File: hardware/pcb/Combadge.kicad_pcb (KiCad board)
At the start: 2 copper layers, 33.7 x 31 mm, 38 parts, among them J1 UART, J2 GND, J3 TOUCH, J4 USB_B_Micro, SW1 CSS-1210TB, SW2 BOOT, U1 TL431DBZ, U2 MCP73831-2-OT, U3 TLV73333PDBV, U4 ESP32-WROOM-32, U5 MAX98357AETE+T

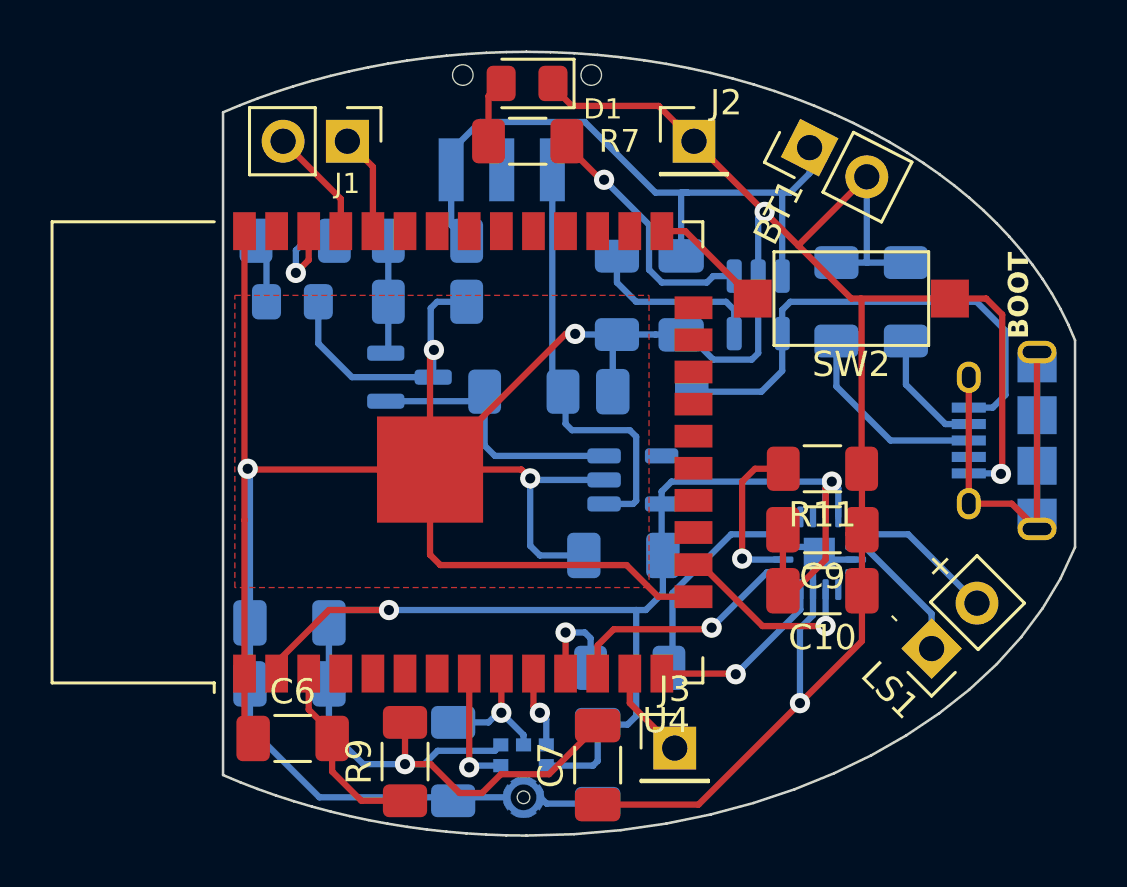
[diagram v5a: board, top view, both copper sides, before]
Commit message: Cleanup silkscreen
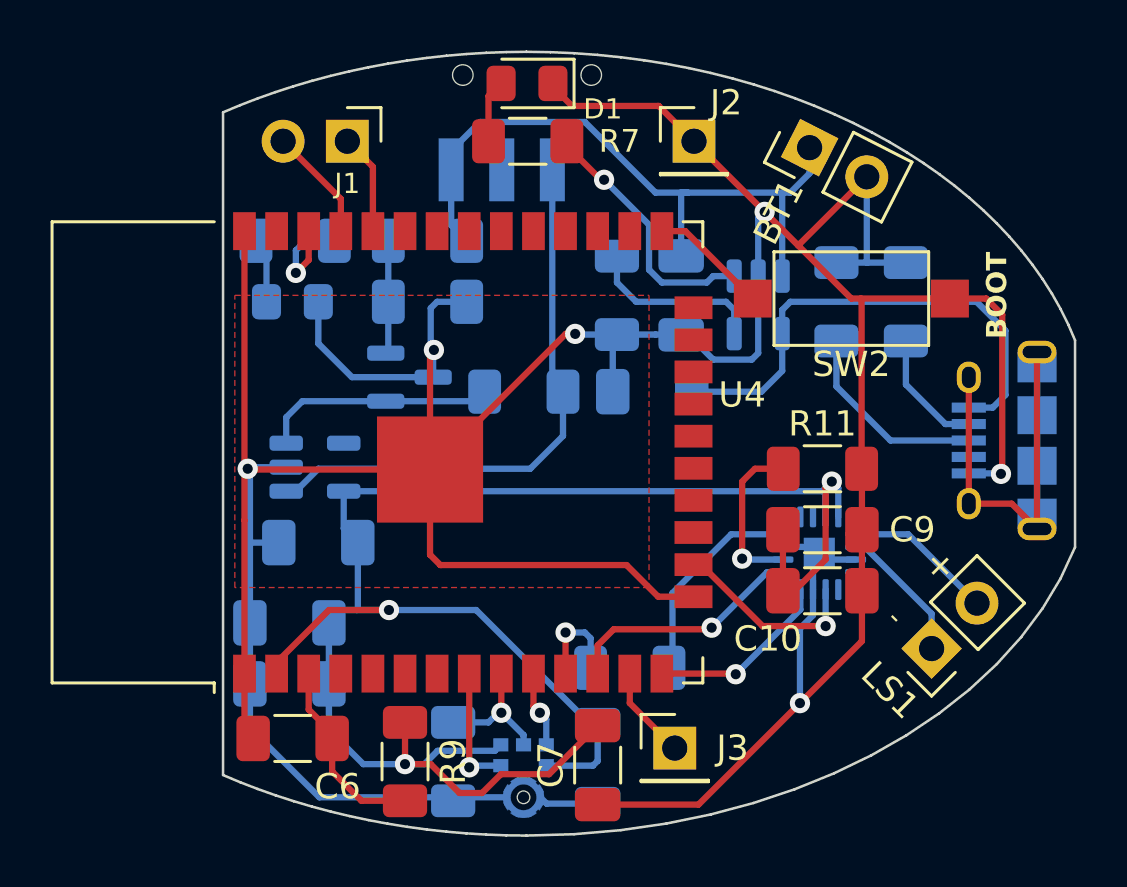
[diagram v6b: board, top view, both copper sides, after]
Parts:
- moved U3 12.6 mm to (147.6, 96.7)
- moved C3 12.1 mm to (147.7, 99.7)
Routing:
- net GND: track 197.2 -> 187.9 mm, vias 7 -> 6
- net +3.3V: track 73.3 -> 80.0 mm
- net Net-(U3-IN): track 17.1 -> 22.6 mm
- net Net-(U1-K): track 11.1 -> 9.29 mm
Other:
- board text added: "*"

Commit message: Add ground pours
Thanks to Reddit user AgentiMi for the recommendation
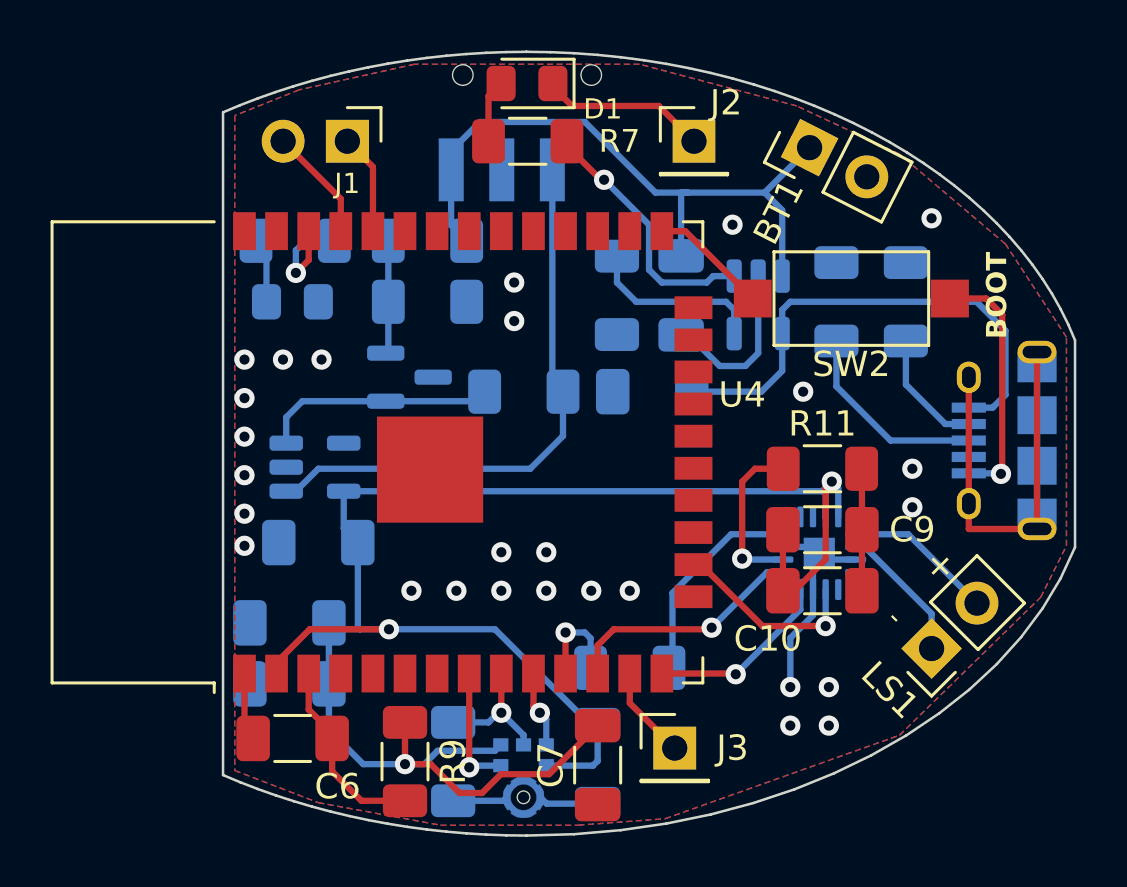
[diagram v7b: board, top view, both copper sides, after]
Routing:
- net GND: track 187.9 -> 48.6 mm, vias 6 -> 28
- net unconnected-(J4-Shield-Pad6): track 20.9 -> 21.5 mm
- added copper zone on B.Cu, net GND

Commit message: Break out ESP enable pin
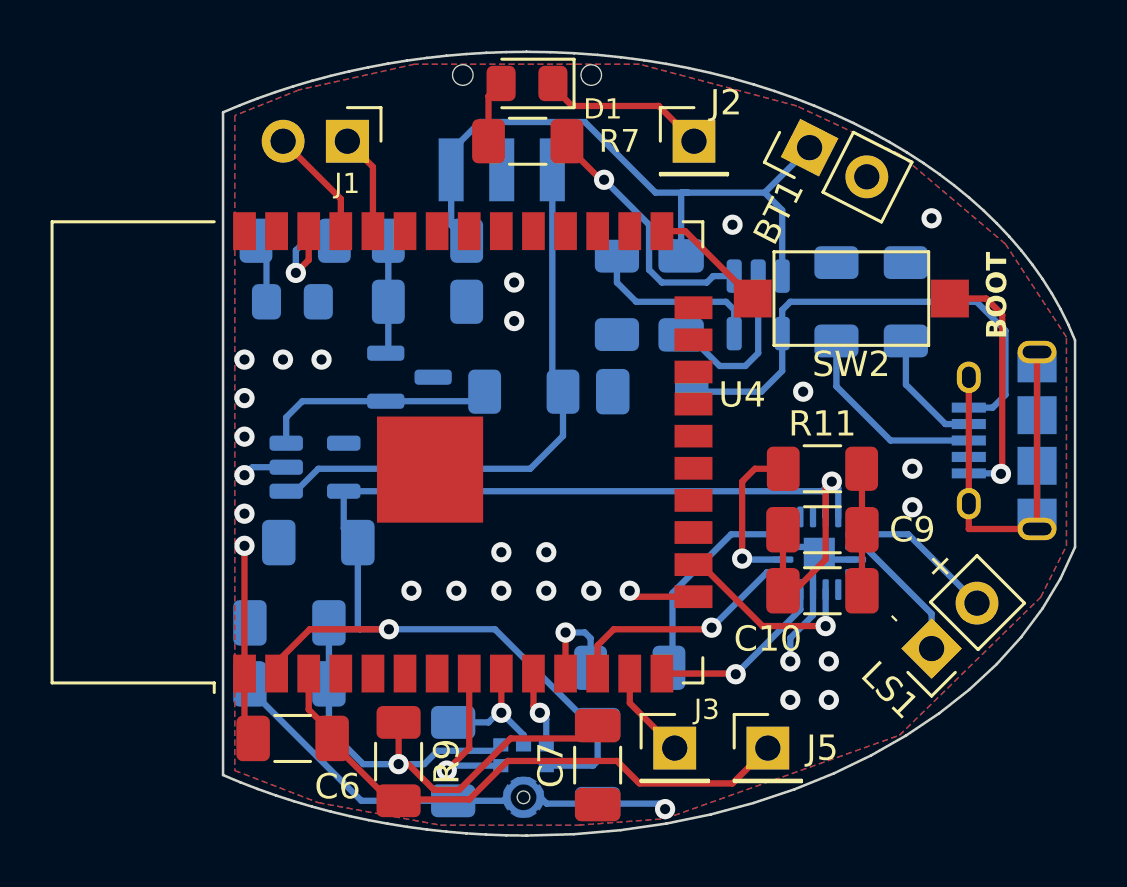
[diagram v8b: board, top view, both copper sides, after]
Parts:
- added J5: ESP_EN, Connector_PinHeader_2.54mm:PinHeader_1x01_P2.54mm_Vertical, F.Cu at (165.5, 107.8)
- moved R9 0.25 mm to (150.9, 108.4)
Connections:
- net Net-(U4-EN) renamed /ESP32/ESP_EN
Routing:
- net GND: track 48.6 -> 69.8 mm, vias 28 -> 29
- net /ESP32/ESP_EN: track 7.62 -> 22.9 mm
- net /ESP32/MIC_BCLK: track 4.98 -> 6.42 mm
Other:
- board text added: "EN"
